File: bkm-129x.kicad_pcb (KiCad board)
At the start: 2 copper layers, 106.7 x 101.1 mm, 128 parts, among them IC010 LM2940CSX-5.0, IC050 LM2990SX-5.0, J001 Conn_02x32_Row_Letter_Last, Q101 2SA1462, Q102 DTA144EKA, Q103 2SC3545, Q201 2SA1462, Q202 DTA144EKA, Q203 2SC3545, Q301 2SA1462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

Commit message: Minor adjustments
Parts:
- added MNT1: TEST_1P, Mounting_Holes:MountingHole_2.7mm_M2.5_DIN965_Pad, F.Cu at (63.2, 152.0)
- added MNT2: TEST_1P, Mounting_Holes:MountingHole_2.7mm_M2.5_DIN965_Pad, F.Cu at (80.4, 57.5)
- added MNT3: TEST_1P, Mounting_Holes:MountingHole_2.7mm_M2.5_DIN965_Pad, F.Cu at (163.3, 57.5)
- added MNT4: TEST_1P, Mounting_Holes:MountingHole_2.7mm_M2.5_DIN965_Pad, F.Cu at (163.3, 152.0)
- added MNT5: TEST_1P, Mounting_Holes:MountingHole_2.7mm_M2.5_DIN965_Pad, F.Cu at (115.1, 104.8)
- moved PBB_IN1 0.51 mm to (63.8, 87.6)
- moved J001 0.13 mm to (156.2, 104.8)
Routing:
- net /-6V: track 34.7 -> 39.6 mm
- net VSSA: track 274.0 -> 272.1 mm
- net VDDA: track 291.5 -> 289.8 mm
- net +5VD: track 90.6 -> 89.3 mm
- net Net-(R106-Pad1): track 48.0 -> 47.0 mm
- net /+6V: track 43.9 -> 44.4 mm

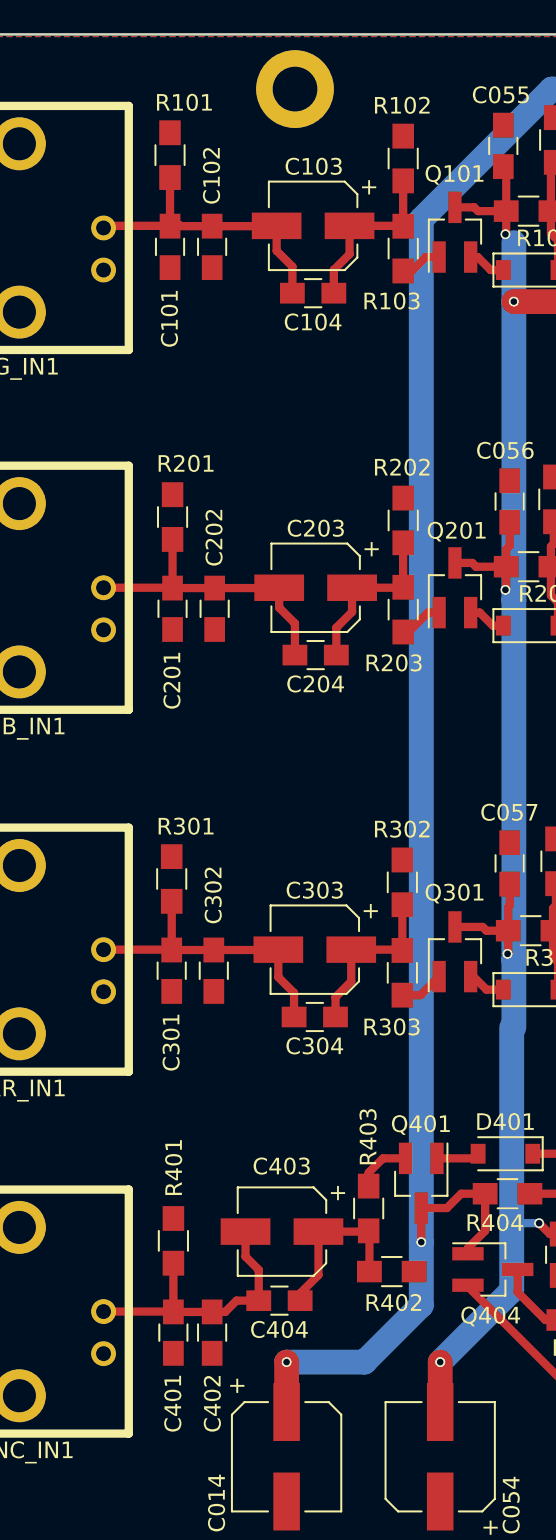
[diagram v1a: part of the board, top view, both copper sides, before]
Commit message: Switched to 8mm caps for video which should fit SMD bipolar ecaps
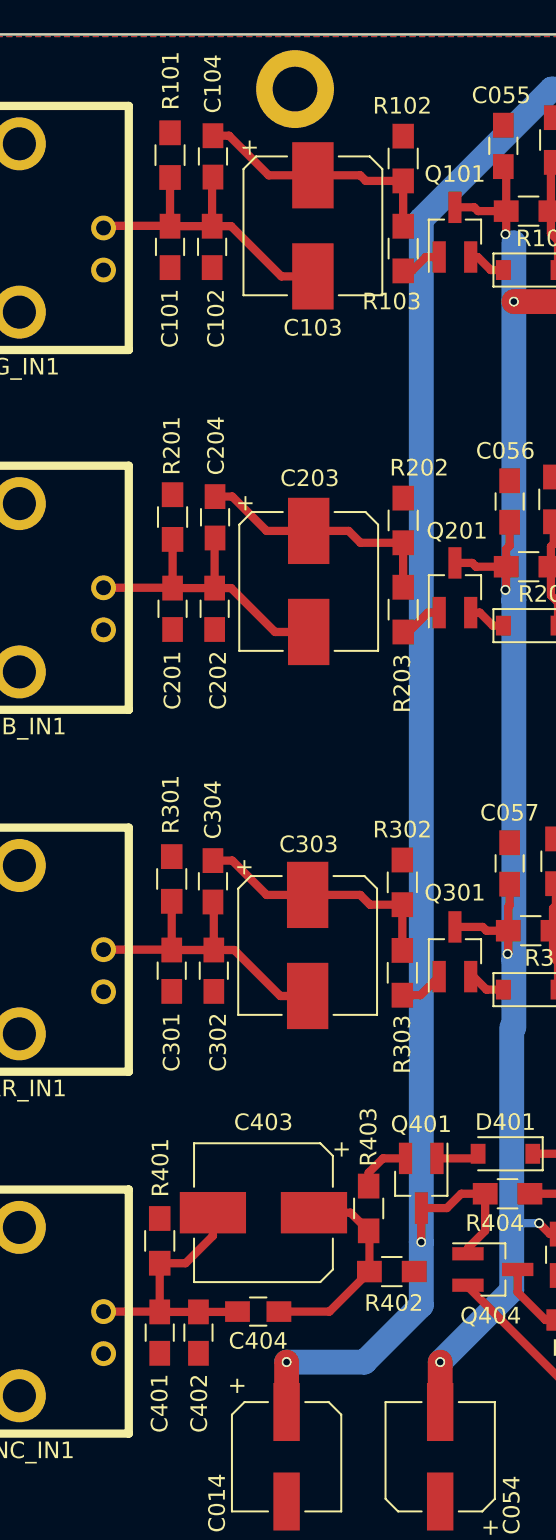
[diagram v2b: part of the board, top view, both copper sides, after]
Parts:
- C103, C203, C303, C403: footprint Capacitors_SMD:CP_Elec_5x5.7 -> Capacitors_SMD:CP_Elec_8x5.4
- moved C204 10.3 mm to (75.6, 83.4), turned to 270 degrees
- moved C304 10.2 mm to (75.4, 105.3), turned to 270 degrees
- moved C104 10.2 mm to (75.4, 61.6), turned to 270 degrees
- moved C403 1.60 mm to (78.5, 125.3)
- moved C404 1.44 mm to (78.2, 131.3)
- moved C402 0.83 mm to (74.6, 132.6)
- moved C401 0.83 mm to (72.2, 132.6)
- moved R401 0.83 mm to (72.2, 127.1)
- moved C203 0.57 mm to (81.2, 87.2), turned to 270 degrees
- moved C303 0.50 mm to (81.2, 109.2), turned to 270 degrees
- turned C103 to 270 degrees
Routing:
- net Net-(C303-Pad1): track 10.3 -> 15.4 mm
- net Net-(C203-Pad1): track 10.2 -> 15.2 mm
- net Net-(C103-Pad1): track 10.4 -> 15.4 mm
- net Net-(C403-Pad1): track 10.1 -> 12.6 mm
- net Net-(C301-Pad1): track 18.0 -> 19.8 mm
- net Net-(C101-Pad1): track 18.1 -> 19.9 mm
- net Net-(C201-Pad1): track 18.1 -> 19.5 mm
- net Net-(C401-Pad1): track 17.1 -> 16.4 mm

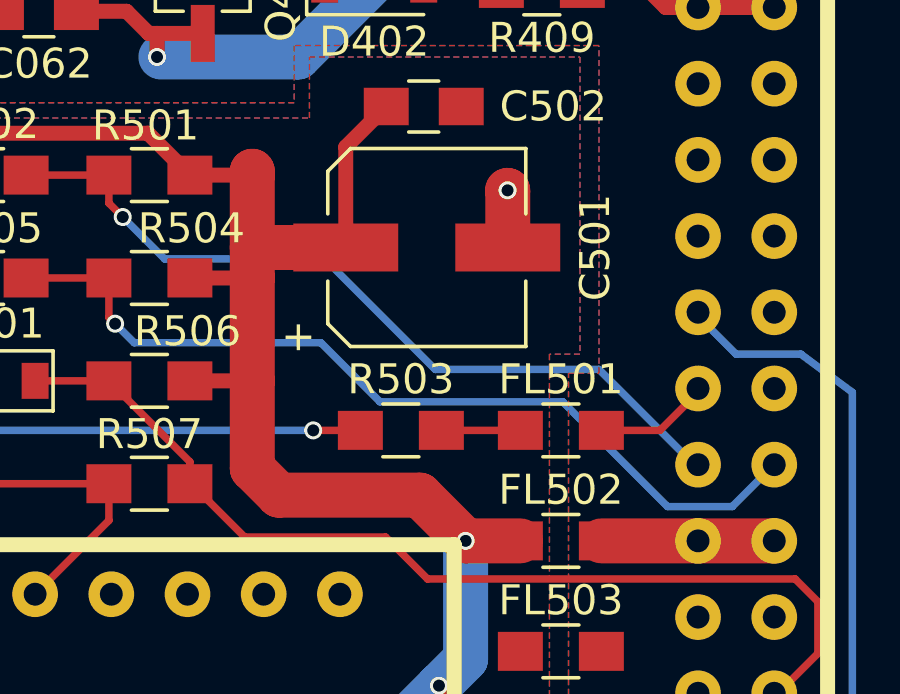
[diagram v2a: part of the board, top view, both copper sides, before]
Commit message: Fixed some footprints
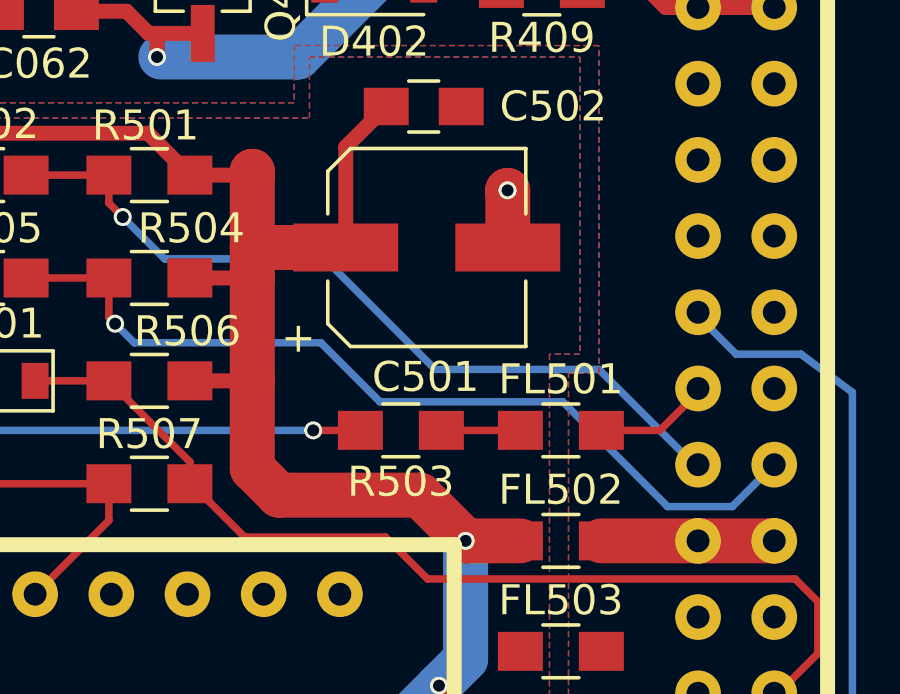
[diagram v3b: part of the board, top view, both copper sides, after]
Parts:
- C501: footprint Capacitors_SMD:CP_Elec_6.3x4.5 -> Capacitors_SMD:CP_Elec_6.3x5.3
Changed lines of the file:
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@@
   )
   (setup
-    (last_trace_width 0.5)
+    (last_trace_width 0.25)
     (user_trace_width 0.5)
     (user_trace_width 1.5)
@@
     )
   )
-  (module Capacitors_SMD:CP_Elec_6.3x4.5 (layer F.Cu)
-    (at 145.8976 126.746)
-    (descr "SMT capacitor, aluminium electrolytic, 6.3x4.5")
-    (attr smd)
-    (fp_text reference C501 (at 5.6134 0 90) (layer F.SilkS)
-      (effects (font (size 1 1) (thickness 0.15)))
-    )
-    (fp_text value 100uF (at 5.4864 0.1524 90) (layer F.Fab)
-      (effects (font (size 1 1) (thickness 0.15)))
-    )
-    (fp_circle (center 0 0) (end 0.9 2.9) (layer F.Fab) (width 0.1))
-    (fp_text user + (at -1.73 -0.08) (layer F.Fab)
-      (effects (font (size 1 1) (thickness 0.15)))
-    )
-    (fp_text user + (at -4.28 2.96) (layer F.SilkS)
-      (effects (font (size 1 1) (thickness 0.15)))
-    )
-    (fp_text user %R (at 0 4.56) (layer F.Fab)
-      (effects (font (size 1 1) (thickness 0.15)))
-    )
-    (fp_line (start 3.15 3.15) (end 3.15 -3.15) (layer F.Fab) (width 0.1))
-    (fp_line (start -2.48 3.15) (end 3.15 3.15) (layer F.Fab) (width 0.1))
-    (fp_line (start -3.15 2.48) (end -2.48 3.15) (layer F.Fab) (width 0.1))
-    (fp_line (start -3.15 -2.48) (end -3.15 2.48) (layer F.Fab) (width 0.1))
-    (fp_line (start -2.48 -3.15) (end -3.15 -2.48) (layer F.Fab) (width 0.1))
-    (fp_line (start 3.15 -3.15) (end -2.48 -3.15) (layer F.Fab) (width 0.1))
-    (fp_line (start 3.3 3.3) (end 3.3 1.12) (layer F.SilkS) (width 0.12))
-    (fp_line (start 3.3 -3.3) (end 3.3 -1.12) (layer F.SilkS) (width 0.12))
-    (fp_line (start -3.3 2.54) (end -3.3 1.12) (layer F.SilkS) (width 0.12))
-    (fp_line (start -3.3 -2.54) (end -3.3 -1.12) (layer F.SilkS) (width 0.12))
-    (fp_line (start 3.3 3.3) (end -2.54 3.3) (layer F.SilkS) (width 0.12))
-    (fp_line (start -2.54 3.3) (end -3.3 2.54) (layer F.SilkS) (width 0.12))
-    (fp_line (start -3.3 -2.54) (end -2.54 -3.3) (layer F.SilkS) (width 0.12))
-    (fp_line (start -2.54 -3.3) (end 3.3 -3.3) (layer F.SilkS) (width 0.12))
-    (fp_line (start -4.7 -3.4) (end 4.7 -3.4) (layer F.CrtYd) (width 0.05))
-    (fp_line (start -4.7 -3.4) (end -4.7 3.4) (layer F.CrtYd) (width 0.05))
-    (fp_line (start 4.7 3.4) (end 4.7 -3.4) (layer F.CrtYd) (width 0.05))
-    (fp_line (start 4.7 3.4) (end -4.7 3.4) (layer F.CrtYd) (width 0.05))
-    (pad 1 smd rect (at -2.7 0 180) (size 3.5 1.6) (layers F.Cu F.Paste F.Mask)
-      (net 1 +5VD))
-    (pad 2 smd rect (at 2.7 0 180) (size 3.5 1.6) (layers F.Cu F.Paste F.Mask)
-      (net 2 GND))
-    (model Capacitors_SMD.3dshapes/CP_Elec_6.3x4.5.wrl
-      (at (xyz 0 0 0))
-      (scale (xyz 1 1 1))
-      (rotate (xyz 0 0 180))
-    )
-  )
   (module Capacitors_SMD:C_0805_HandSoldering (layer F.Cu)
     (at 145.796 122.047)
@@
     (tags "resistor 0805")
     (attr smd)
-    (fp_text reference R503 (at 0 -1.7) (layer F.SilkS)
+    (fp_text reference R503 (at 0 1.7145) (layer F.SilkS)
       (effects (font (size 1 1) (thickness 0.15)))
     )
@@
       (at (xyz 0 0 0))
       (scale (xyz 1 1 1))
+      (rotate (xyz 0 0 180))
+    )
+  )
+  (module Capacitors_SMD:CP_Elec_6.3x5.3 (layer F.Cu)
+    (at 145.8976 126.746)
+    (descr "SMT capacitor, aluminium electrolytic, 6.3x5.3")
+    (attr smd)
+    (fp_text reference C501 (at -0.0381 4.318) (layer F.SilkS)
+      (effects (font (size 1 1) (thickness 0.15)))
+    )
+    (fp_text value 100uF (at 0 -4.56) (layer F.Fab)
+      (effects (font (size 1 1) (thickness 0.15)))
+    )
+    (fp_circle (center 0 0) (end 0.6 3) (layer F.Fab) (width 0.1))
+    (fp_text user + (at -1.75 -0.08) (layer F.Fab)
+      (effects (font (size 1 1) (thickness 0.15)))
+    )
+    (fp_text user + (at -4.28 3.01) (layer F.SilkS)
+      (effects (font (size 1 1) (thickness 0.15)))
+    )
+    (fp_text user %R (at 0 4.56) (layer F.Fab)
+      (effects (font (size 1 1) (thickness 0.15)))
+    )
+    (fp_line (start 3.15 3.15) (end 3.15 -3.15) (layer F.Fab) (width 0.1))
+    (fp_line (start -2.48 3.15) (end 3.15 3.15) (layer F.Fab) (width 0.1))
+    (fp_line (start -3.15 2.48) (end -2.48 3.15) (layer F.Fab) (width 0.1))
+    (fp_line (start -3.15 -2.48) (end -3.15 2.48) (layer F.Fab) (width 0.1))
+    (fp_line (start -2.48 -3.15) (end -3.15 -2.48) (layer F.Fab) (width 0.1))
+    (fp_line (start 3.15 -3.15) (end -2.48 -3.15) (layer F.Fab) (width 0.1))
+    (fp_line (start 3.3 3.3) (end 3.3 1.12) (layer F.SilkS) (width 0.12))
+    (fp_line (start 3.3 -3.3) (end 3.3 -1.12) (layer F.SilkS) (width 0.12))
+    (fp_line (start -3.3 2.54) (end -3.3 1.12) (layer F.SilkS) (width 0.12))
+    (fp_line (start -3.3 -2.54) (end -3.3 -1.12) (layer F.SilkS) (width 0.12))
+    (fp_line (start 3.3 3.3) (end -2.54 3.3) (layer F.SilkS) (width 0.12))
+    (fp_line (start -2.54 3.3) (end -3.3 2.54) (layer F.SilkS) (width 0.12))
+    (fp_line (start -3.3 -2.54) (end -2.54 -3.3) (layer F.SilkS) (width 0.12))
+    (fp_line (start -2.54 -3.3) (end 3.3 -3.3) (layer F.SilkS) (width 0.12))
+    (fp_line (start -4.7 -3.4) (end 4.7 -3.4) (layer F.CrtYd) (width 0.05))
+    (fp_line (start -4.7 -3.4) (end -4.7 3.4) (layer F.CrtYd) (width 0.05))
+    (fp_line (start 4.7 3.4) (end 4.7 -3.4) (layer F.CrtYd) (width 0.05))
+    (fp_line (start 4.7 3.4) (end -4.7 3.4) (layer F.CrtYd) (width 0.05))
+    (pad 1 smd rect (at -2.7 0 180) (size 3.5 1.6) (layers F.Cu F.Paste F.Mask)
+      (net 1 +5VD))
+    (pad 2 smd rect (at 2.7 0 180) (size 3.5 1.6) (layers F.Cu F.Paste F.Mask)
+      (net 2 GND))
+    (model Capacitors_SMD.3dshapes/CP_Elec_6.3x5.3.wrl
+      (at (xyz 0 0 0))
+      (scale (xyz 1 1 1))

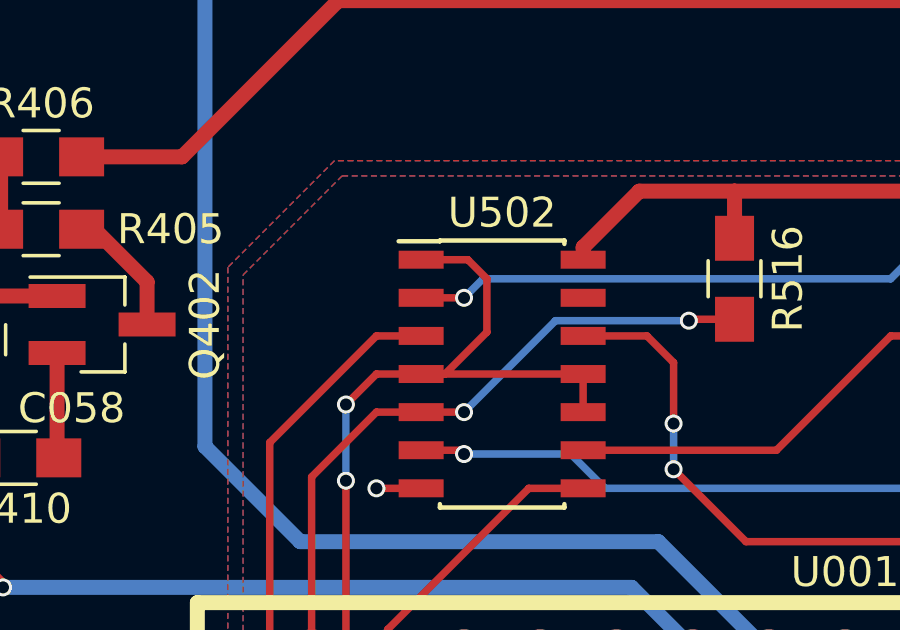
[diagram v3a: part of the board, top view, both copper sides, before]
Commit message: Added missing pullup resistor on SCLK
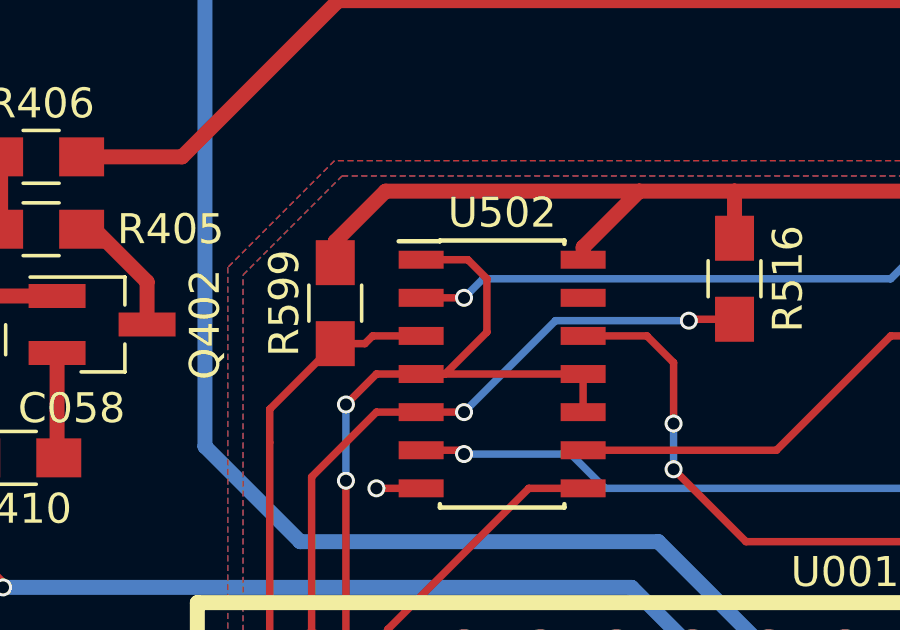
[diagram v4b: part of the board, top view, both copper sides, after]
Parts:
- added R599: 4.7k, Resistors_SMD:R_0805_HandSoldering, F.Cu at (108.2, 126.7)
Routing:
- net +5VD: track 89.3 -> 100.8 mm
- net Net-(R599-Pad1): track 29.3 -> 30.0 mm
